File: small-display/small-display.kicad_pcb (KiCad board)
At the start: 4 copper layers, 43 x 62 mm, 44 parts, among them J1 2047110001, J2 Micro_SD_Card_Det, J5 F32D-1A7Y1-21040, U1 TPD4EUSB30, U2 74LVC1G07SE-7, U3 RT9742GGJ5, U4 PAM2804AAB010, U5 USB2412-DZK, U6 NLVVHC1G04DFT1G, U7 M24M01-DFDW6TP, Y1 ECS-240-8-33-AGN-TR

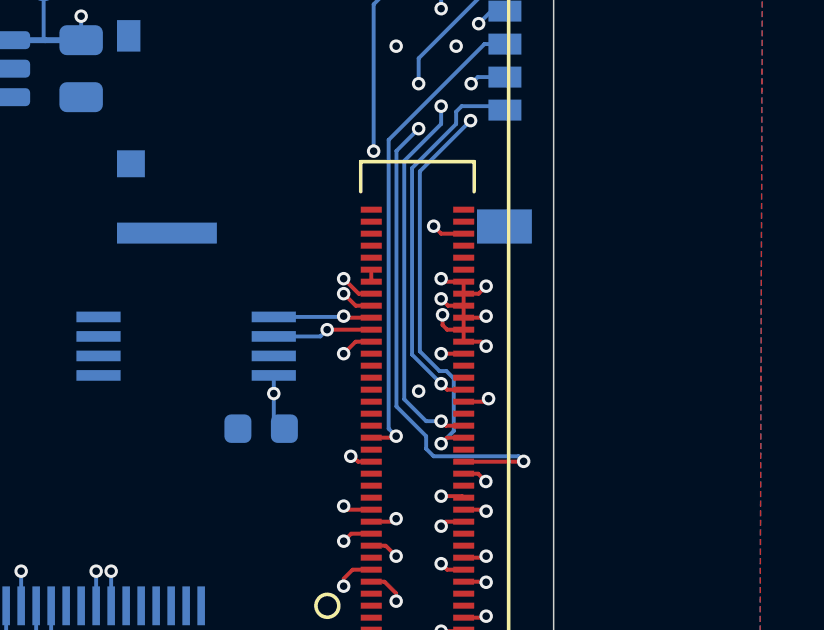
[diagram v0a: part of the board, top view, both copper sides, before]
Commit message: More routing improvements.
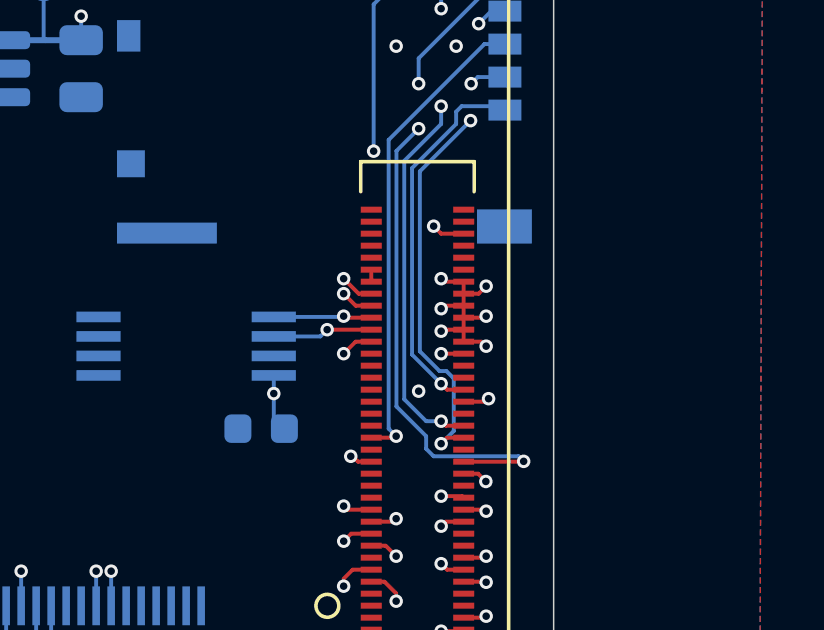
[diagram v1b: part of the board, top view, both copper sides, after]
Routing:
- net /LED_A: track 49.3 -> 51.3 mm
- net Net-(L1-Pad1): track 54.6 -> 55.6 mm
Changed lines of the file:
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@@
   (via (at 40.8305 22) (size 0.45) (drill 0.25) (layers "F.Cu" "B.Cu") (net 34))
   (via (at 37 13.75) (size 0.45) (drill 0.25) (layers "F.Cu" "B.Cu") (net 34))
-  (segment (start 37 17.5) (end 37 13.75) (width 0.13) (layer "In1.Cu") (net 34))
-  (segment (start 40.75 21.9195) (end 40.75 21.25) (width 0.13) (layer "In1.Cu") (net 34))
-  (segment (start 40.8305 22) (end 40.75 21.9195) (width 0.13) (layer "In1.Cu") (net 34))
-  (segment (start 40.75 21.25) (end 37 17.5) (width 0.13) (layer "In1.Cu") (net 34))
+  (segment (start 37 19) (end 37 13.75) (width 0.13) (layer "In1.Cu") (net 34))
+  (segment (start 38.92 20.92) (end 37 19) (width 0.13) (layer "In1.Cu") (net 34))
+  (segment (start 40.8305 22) (end 39.7505 20.92) (width 0.13) (layer "In1.Cu") (net 34))
+  (segment (start 39.7505 20.92) (end 38.92 20.92) (width 0.13) (layer "In1.Cu") (net 34))
   (segment (start 37 8.855) (end 37 13.75) (width 0.13) (layer "B.Cu") (net 34))
   (segment (start 41.175 4.68) (end 37 8.855) (width 0.13) (layer "B.Cu") (net 34))
@@
   (segment (start 40 18.1) (end 40 20.1) (width 0.13) (layer "F.Cu") (net 126))
   (segment (start 40.5 18.5) (end 40 18.5) (width 0.13) (layer "F.Cu") (net 126))
-  (segment (start 39.25 18.671632) (end 39.478368 18.9) (width 0.13) (layer "F.Cu") (net 126))
+  (segment (start 39.25 19) (end 39.35 18.9) (width 0.13) (layer "F.Cu") (net 126))
   (segment (start 39.35 18.1) (end 40 18.1) (width 0.13) (layer "F.Cu") (net 126))
   (segment (start 20.25 59.255) (end 20.25 60) (width 0.2) (layer "F.Cu") (net 126))
   (segment (start 22.75 57.745) (end 22.75 57) (width 0.2) (layer "F.Cu") (net 126))
-  (segment (start 39.478368 18.9) (end 40 18.9) (width 0.13) (layer "F.Cu") (net 126))
-  (segment (start 39.45 19.7) (end 40 19.7) (width 0.13) (layer "F.Cu") (net 126))
   (segment (start 20.25 57.745) (end 20.25 57) (width 0.2) (layer "F.Cu") (net 126))
   (segment (start 40 19.3) (end 40.7 19.3) (width 0.13) (layer "F.Cu") (net 126))
-  (segment (start 39.296632 19.546632) (end 39.45 19.7) (width 0.13) (layer "F.Cu") (net 126))
-  (segment (start 39.296632 19.203368) (end 39.296632 19.546632) (width 0.13) (layer "F.Cu") (net 126))
+  (segment (start 39.25 19.75) (end 39.4 19.75) (width 0.13) (layer "F.Cu") (net 126))
   (segment (start 40.7 19.3) (end 40.75 19.25) (width 0.13) (layer "F.Cu") (net 126))
+  (segment (start 39.45 19.7) (end 40 19.7) (width 0.13) (layer "F.Cu") (net 126))
   (segment (start 40.75 20.25) (end 40.6 20.1) (width 0.13) (layer "F.Cu") (net 126))
+  (segment (start 39.4 19.75) (end 39.45 19.7) (width 0.13) (layer "F.Cu") (net 126))
   (segment (start 40.6 20.1) (end 40 20.1) (width 0.13) (layer "F.Cu") (net 126))
   (segment (start 39.25 18) (end 39.35 18.1) (width 0.13) (layer "F.Cu") (net 126))
+  (segment (start 39.35 18.9) (end 40 18.9) (width 0.13) (layer "F.Cu") (net 126))
   (via (at 17.5 25.75) (size 0.45) (drill 0.25) (layers "F.Cu" "B.Cu") (net 126))
   (via (at 40.75 19.25) (size 0.45) (drill 0.25) (layers "F.Cu" "B.Cu") (net 126))
   (via (at 20.25 60) (size 0.45) (drill 0.25) (layers "F.Cu" "B.Cu") (net 126))
   (via (at 22.75 60) (size 0.45) (drill 0.25) (layers "F.Cu" "B.Cu") (net 126))
-  (via (at 39.296632 19.203368) (size 0.45) (drill 0.25) (layers "F.Cu" "B.Cu") (net 126))
+  (via (at 39.25 19.75) (size 0.45) (drill 0.25) (layers "F.Cu" "B.Cu") (net 126))
   (via (at 40.75 18.25) (size 0.45) (drill 0.25) (layers "F.Cu" "B.Cu") (net 126))
   (via (at 31.75 59) (size 0.45) (drill 0.25) (layers "F.Cu" "B.Cu") (net 126))
@@
   (via (at 22.75 57) (size 0.45) (drill 0.25) (layers "F.Cu" "B.Cu") (net 126))
   (via (at 40.75 20.25) (size 0.45) (drill 0.25) (layers "F.Cu" "B.Cu") (net 126))
-  (via (at 39.25 18.671632) (size 0.45) (drill 0.25) (layers "F.Cu" "B.Cu") (net 126))
+  (via (at 39.25 19) (size 0.45) (drill 0.25) (layers "F.Cu" "B.Cu") (net 126))
   (segment (start 16.4525 25.7975) (end 16.5 25.75) (width 0.5) (layer "B.Cu") (net 126))
   (segment (start 17 25.75) (end 17.5 25.75) (width 0.5) (layer "B.Cu") (net 126))
@@
   (via (at 36 56.5) (size 0.45) (drill 0.25) (layers "F.Cu" "B.Cu") (net 127))
   (segment (start 29.25 55.5) (end 36 55.5) (width 0.5) (layer "In2.Cu") (net 127))
+  (segment (start 36 55.5) (end 36 56.5) (width 0.5) (layer "In2.Cu") (net 127))
   (segment (start 13 31) (end 13 39.25) (width 0.5) (layer "In2.Cu") (net 127))
   (segment (start 13 39.25) (end 29.25 55.5) (width 0.5) (layer "In2.Cu") (net 127))
+  (segment (start 13 31) (end 13 30) (width 0.5) (layer "In2.Cu") (net 127))
   (segment (start 12.75 28.9047) (end 12.75 26.675) (width 0.13) (layer "B.Cu") (net 127))
   (segment (start 12 25.875) (end 12 24.25) (width 0.13) (layer "B.Cu") (net 127))
+  (segment (start 13 30) (end 13 31) (width 0.5) (layer "B.Cu") (net 127))
   (segment (start 12.75 26.675) (end 12.775 26.65) (width 0.13) (layer "B.Cu") (net 127))
   (segment (start 12.75 28.9047) (end 12.75 29.75) (width 0.13) (layer "B.Cu") (net 127))
   (segment (start 12.75 29.75) (end 13 30) (width 0.5) (layer "B.Cu") (net 127))
-  (segment (start 13 30) (end 13 31) (width 0.5) (layer "B.Cu") (net 127))
   (segment (start 12.775 26.65) (end 12 25.875) (width 0.13) (layer "B.Cu") (net 127))
   (segment (start 7.55 24.3775) (end 7.55 26.1025) (width 0.13) (layer "B.Cu") (net 128))
@@
   (segment (start 14 26) (end 14 39) (width 0.5) (layer "In2.Cu") (net 158))
   (segment (start 37.25 54.75) (end 38 55.5) (width 0.5) (layer "In2.Cu") (net 158))
+  (segment (start 38 55.5) (end 38 56.5) (width 0.5) (layer "In2.Cu") (net 158))
   (segment (start 29.75 54.75) (end 37.25 54.75) (width 0.5) (layer "In2.Cu") (net 158))
   (segment (start 16.75 23.25) (end 14 26) (width 0.5) (layer "In2.Cu") (net 158))
@@
   )
   (zone (net 170) (net_name "+3.3V") (layer "In1.Cu") (hatch edge 0.508)
-    (connect_pads (clearance 0.508))
-    (min_thickness 0.254)
-    (fill yes (thermal_gap 0.508) (thermal_bridge_width 0.508))
+    (connect_pads (clearance 0.13))
+    (min_thickness 0.13)
+    (fill yes (thermal_gap 0.13) (thermal_bridge_width 0.13))
     (polygon
       (pts
@@
   )
   (zone (net 126) (net_name "+5V") (layer "In2.Cu") (hatch edge 0.508)
-    (connect_pads (clearance 0.508))
-    (min_thickness 0.254)
-    (fill yes (thermal_gap 0.508) (thermal_bridge_width 0.508))
+    (connect_pads (clearance 0.13))
+    (min_thickness 0.13)
+    (fill yes (thermal_gap 0.13) (thermal_bridge_width 0.13))
     (polygon
       (pts

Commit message: More or less complete except for DRC.
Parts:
- added R10: 10k, Resistor_SMD:R_0402_1005Metric, B.Cu at (25.2, 15.0)
- added TP13: TestPoint, TestPoint:TestPoint_Pad_D1.0mm, B.Cu at (4.50, 44.2)
- moved TP3 28.0 mm to (7.25, 44.2)
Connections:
- Module1 pad 101: USBOTG_ID -> GND
- Module1 pad 102: /PCIE_CLK_nREQ -> unconnected-(Module1-Pad102)
- Module1 pad 109: PCIE_nRST -> unconnected-(Module1-Pad109)
- Module1 pad 11: TRD2_P -> unconnected-(Module1-Pad11)
- Module1 pad 110: /PCIE_CLK_P -> unconnected-(Module1-Pad110)
- Module1 pad 111: TV_OUT -> unconnected-(Module1-Pad111)
- Module1 pad 112: /PCIE_CLK_N -> unconnected-(Module1-Pad112)
- Module1 pad 115: CAM1_D0_N -> unconnected-(Module1-Pad115)
- Module1 pad 116: /PCIE_RX_P -> unconnected-(Module1-Pad116)
- Module1 pad 117: CAM1_D0_P -> unconnected-(Module1-Pad117)
- Module1 pad 118: /PCIE_RX_N -> unconnected-(Module1-Pad118)
- Module1 pad 121: CAM1_D1_N -> unconnected-(Module1-Pad121)
- Module1 pad 122: /PCIE_TX_P -> unconnected-(Module1-Pad122)
- Module1 pad 123: CAM1_D1_P -> unconnected-(Module1-Pad123)
- Module1 pad 124: /PCIE_TX_N -> unconnected-(Module1-Pad124)
- Module1 pad 127: CAM1_C_N -> unconnected-(Module1-Pad127)
- Module1 pad 128: /CAM0_D0_N -> unconnected-(Module1-Pad128)
- Module1 pad 129: CAM1_C_P -> unconnected-(Module1-Pad129)
- Module1 pad 130: /CAM0_D0_P -> unconnected-(Module1-Pad130)
- Module1 pad 133: CAM1_D2_N -> unconnected-(Module1-Pad133)
- Module1 pad 134: /CAM0_D1_N -> unconnected-(Module1-Pad134)
- Module1 pad 135: CAM1_D2_P -> unconnected-(Module1-Pad135)
- Module1 pad 136: /CAM0_D1_P -> unconnected-(Module1-Pad136)
- Module1 pad 139: CAM1_D3_N -> unconnected-(Module1-Pad139)
- Module1 pad 140: /CAM0_C_N -> unconnected-(Module1-Pad140)
- Module1 pad 141: CAM1_D3_P -> unconnected-(Module1-Pad141)
- Module1 pad 142: /CAM0_C_P -> unconnected-(Module1-Pad142)
- Module1 pad 143: HDMI1_HOTPLUG -> unconnected-(Module1-Pad143)
- Module1 pad 145: HDMI1_SDA -> unconnected-(Module1-Pad145)
- Module1 pad 146: /HDMI1_D2_P -> unconnected-(Module1-Pad146)
- Module1 pad 147: HDMI1_SCL -> unconnected-(Module1-Pad147)
- Module1 pad 148: /HDMI1_D2_N -> unconnected-(Module1-Pad148)
- Module1 pad 149: HDMI1_CEC -> unconnected-(Module1-Pad149)
- Module1 pad 15: ETH_LEDY -> unconnected-(Module1-Pad15)
- Module1 pad 151: HDMI0_CEC -> unconnected-(Module1-Pad151)
- Module1 pad 152: /HDMI1_D1_P -> unconnected-(Module1-Pad152)
- Module1 pad 153: HDMI0_HOTPLUG -> unconnected-(Module1-Pad153)
- Module1 pad 154: /HDMI1_D1_N -> unconnected-(Module1-Pad154)
- Module1 pad 157: DSI0_D0_N -> unconnected-(Module1-Pad157)
- Module1 pad 158: /HDMI1_D0_P -> unconnected-(Module1-Pad158)
- Module1 pad 159: DSI0_D0_P -> unconnected-(Module1-Pad159)
- Module1 pad 160: /HDMI1_D0_N -> unconnected-(Module1-Pad160)
- Module1 pad 163: DSI0_D1_N -> unconnected-(Module1-Pad163)
- Module1 pad 164: /HDMI1_CK_P -> unconnected-(Module1-Pad164)
- Module1 pad 165: DSI0_D1_P -> unconnected-(Module1-Pad165)
- Module1 pad 166: /HDMI1_CK_N -> unconnected-(Module1-Pad166)
- Module1 pad 169: DSI0_C_N -> unconnected-(Module1-Pad169)
- Module1 pad 17: ETH_LEDG -> unconnected-(Module1-Pad17)
- Module1 pad 170: /HDMI0_D2_P -> unconnected-(Module1-Pad170)
- Module1 pad 171: DSI0_C_P -> unconnected-(Module1-Pad171)
- Module1 pad 172: /HDMI0_D2_N -> unconnected-(Module1-Pad172)
- Module1 pad 175: DSI1_D0_N -> unconnected-(Module1-Pad175)
- Module1 pad 176: /HDMI0_D1_P -> unconnected-(Module1-Pad176)
- Module1 pad 177: DSI1_D0_P -> unconnected-(Module1-Pad177)
- Module1 pad 178: /HDMI0_D1_N -> unconnected-(Module1-Pad178)
- Module1 pad 181: DSI1_D1_N -> unconnected-(Module1-Pad181)
- Module1 pad 182: /HDMI0_D0_P -> unconnected-(Module1-Pad182)
- Module1 pad 183: DSI1_D1_P -> unconnected-(Module1-Pad183)
- Module1 pad 184: /HDMI0_D0_N -> unconnected-(Module1-Pad184)
- Module1 pad 187: DSI1_C_N -> unconnected-(Module1-Pad187)
- Module1 pad 188: /HDMI0_CK_P -> unconnected-(Module1-Pad188)
- Module1 pad 189: DSI1_C_P -> unconnected-(Module1-Pad189)
- Module1 pad 190: /HDMI0_CK_N -> unconnected-(Module1-Pad190)
- Module1 pad 193: DSI1_D2_N -> unconnected-(Module1-Pad193)
- Module1 pad 194: /DSI1_D3_N -> unconnected-(Module1-Pad194)
- Module1 pad 195: DSI1_D2_P -> unconnected-(Module1-Pad195)
- Module1 pad 196: /DSI1_D3_P -> unconnected-(Module1-Pad196)
- Module1 pad 199: HDMI0_SDA -> unconnected-(Module1-Pad199)
- Module1 pad 200: /HDMI0_SCL -> unconnected-(Module1-Pad200)
- Module1 pad 3: TRD3_P -> unconnected-(Module1-Pad3)
- Module1 pad 30: GPIO6 -> unconnected-(Module1-Pad30)
- Module1 pad 33: GND -> unconnected-(Module1-Pad33)
- Module1 pad 34: GPIO5 -> unconnected-(Module1-Pad34)
- Module1 pad 35: ID_SC -> unconnected-(Module1-Pad35)
- Module1 pad 36: ID_SD -> unconnected-(Module1-Pad36)
- Module1 pad 45: GPIO24 -> unconnected-(Module1-Pad45)
- Module1 pad 5: TRD3_N -> unconnected-(Module1-Pad5)
- Module1 pad 54: GPIO4 -> unconnected-(Module1-Pad54)
- Module1 pad 56: GPIO3 -> unconnected-(Module1-Pad56)
- Module1 pad 9: TRD2_N -> unconnected-(Module1-Pad9)
- Module1 pad 92: RUN_PG -> unconnected-(Module1-Pad92)
- Module1 pad 93: unconnected-(Module1-Pad93) -> /nRPIBOOT
- Module1 pad 94: AIN1 -> unconnected-(Module1-Pad94)
- Module1 pad 96: AIN0 -> unconnected-(Module1-Pad96)
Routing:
- net /nRPIBOOT: track 0.00 -> 15.6 mm, vias 0 -> 1
- net +3.3V: track 21.0 -> 23.0 mm, vias 18 -> 20
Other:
- board text removed: "LED indicators (move to front)"

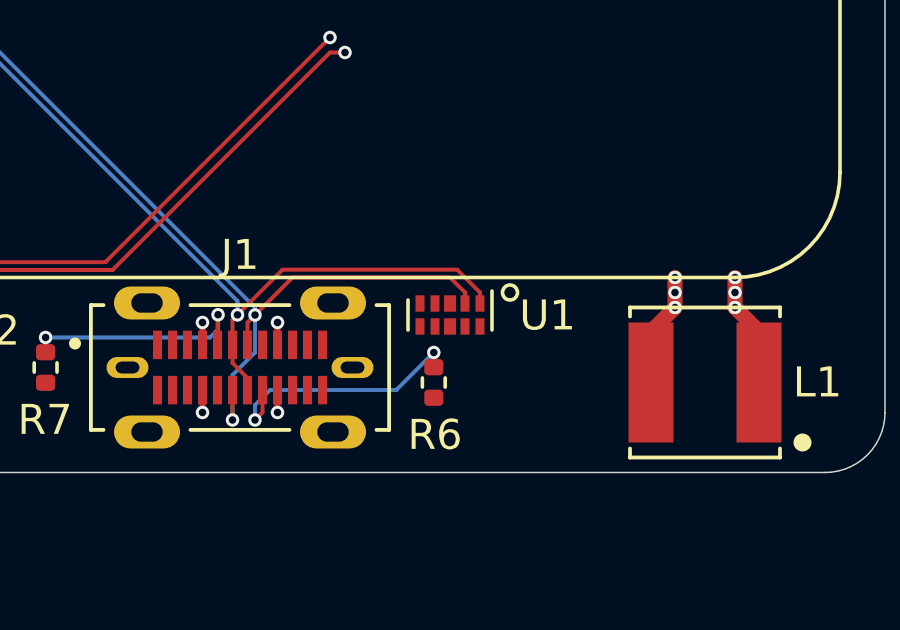
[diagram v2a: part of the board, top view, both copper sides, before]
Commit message: Tweaking silk screen.
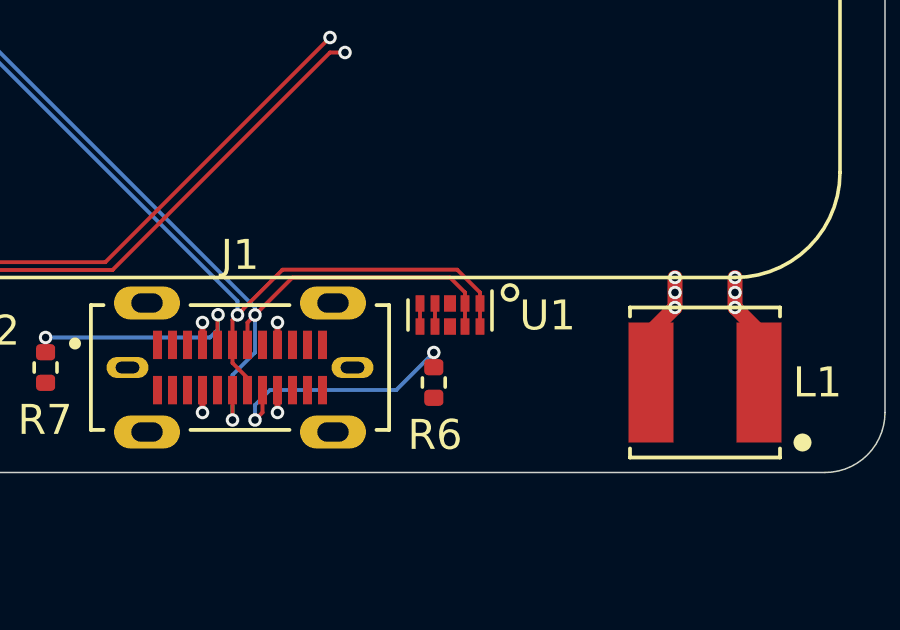
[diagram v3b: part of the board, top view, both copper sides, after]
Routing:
- net unconnected-(U1-Pad5): track 0.00 -> 0.77 mm
- net unconnected-(U1-Pad4): track 0.00 -> 0.77 mm
- net USBD_P: track 59.3 -> 60.1 mm
- net USBD_N: track 61.6 -> 62.4 mm
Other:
- board text removed: "I2C memory"
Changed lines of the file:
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@@
     (property "Sheetname" "")
     (attr through_hole)
-    (fp_text reference "J2" (at 8 5.75 180) (layer "B.SilkS")
-      (effects (font (size 1.000685 1.000685) (thickness 0.015)) (justify mirror))
+    (fp_text reference "J2" (at 8 3.25 180) (layer "B.SilkS")
+      (effects (font (size 1.000685 1.000685) (thickness 0.15)) (justify mirror))
     )
     (fp_text value "Micro_SD_Card_Det" (at 3.719055 -8.349145 90) (layer "B.Fab")
@@
   (gr_arc (start 2 62) (mid 0.585786 61.414214) (end 0 60) (layer "Edge.Cuts") (width 0.05))
   (gr_line (start 43 2) (end 43 60) (layer "Edge.Cuts") (width 0.05))
-  (gr_text "I2C memory" (at -40 -10) (layer "B.SilkS")
-    (effects (font (size 1.5 1.5) (thickness 0.3)) (justify mirror))
-  )
   (gr_text "FPC" (at 39.5 48) (layer "B.SilkS")
     (effects (font (size 1 1) (thickness 0.15)) (justify mirror))
@@
   (segment (start 21.25 56.911997) (end 21.25 57.745) (width 0.13) (layer "F.Cu") (net 16))
   (segment (start 21.58 56.581997) (end 21.58 56.57603) (width 0.13) (layer "F.Cu") (net 16))
+  (segment (start 29.5 56.365) (end 29.5 57.135) (width 0.13) (layer "F.Cu") (net 16))
   (segment (start 21.75 58.85) (end 21.75 59.255) (width 0.13) (layer "F.Cu") (net 16))
   (segment (start 28.74 55.24) (end 29.5 56) (width 0.13) (layer "F.Cu") (net 16))
@@
   (segment (start 4.5 41) (end 4.5 40.75) (width 0.13) (layer "B.Cu") (net 16))
   (segment (start 29 56) (end 29 56.365) (width 0.13) (layer "F.Cu") (net 17))
+  (segment (start 29 56.365) (end 29 57.135) (width 0.13) (layer "F.Cu") (net 17))
   (segment (start 23.25 55.5) (end 28.5 55.5) (width 0.13) (layer "F.Cu") (net 17))
   (segment (start 22 56.75) (end 23.25 55.5) (width 0.13) (layer "F.Cu") (net 17))
@@
   (segment (start 15.5 22) (end 16.000001 21.999999) (width 0.13) (layer "B.Cu") (net 147))
   (segment (start 14.5 22.01) (end 15.49 22.01) (width 0.13) (layer "B.Cu") (net 147))
+  (segment (start 28 56.365) (end 28 57.135) (width 0.13) (layer "F.Cu") (net 148))
+  (segment (start 27.5 56.365) (end 27.5 57.135) (width 0.13) (layer "F.Cu") (net 149))
   (segment (start 5 15.565) (end 5 14.025) (width 0.13) (layer "B.Cu") (net 150))
   (segment (start 5 14.025) (end 5.025 14) (width 0.13) (layer "B.Cu") (net 150))
